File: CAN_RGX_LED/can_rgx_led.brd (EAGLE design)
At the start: 240 x 13 mm, 9 parts

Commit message: board 1_0
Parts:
- added R1: 22M, SparkFun-Resistors:0603
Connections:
- new net N$8: R1.1, U$1.P$2
- net +: now also R1.2; no longer U$1.P$2
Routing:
- added copper zone on layer 1, net N$8
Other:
- board text added: "+"
- board text added: "-"
- board text added: "uORocketry CAN-RGX-24V v1.0"

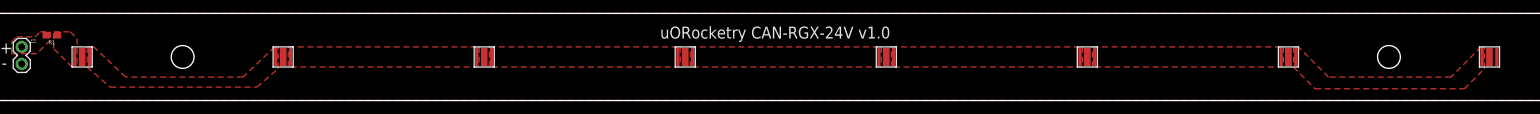
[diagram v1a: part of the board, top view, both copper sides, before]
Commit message: switch LED package
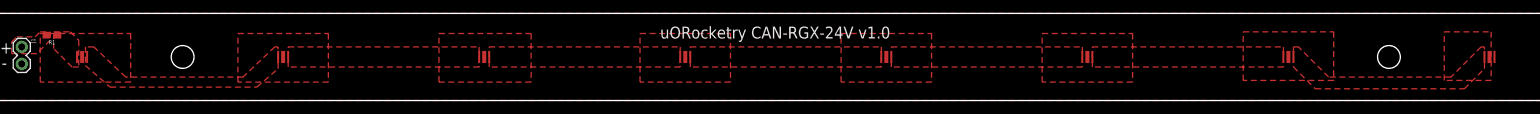
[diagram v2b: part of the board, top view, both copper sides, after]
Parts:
- U$1, U$2, U$3, U$4, U$5, U$6, U$7, U$8: value OSLONSSL150 -> LUXEON-CZ; device uORocketry-parts:OSLONSSL150 -> uORocketry-parts:LUXEON-CZ
- turned U$1 to 0 degrees
- turned U$2 to 0 degrees
- turned U$3 to 0 degrees
- turned U$4 to 0 degrees
- turned U$5 to 0 degrees
- turned U$6 to 0 degrees
- turned U$7 to 0 degrees
- turned U$8 to 0 degrees
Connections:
- new net N$1: U$3.P$1
- new net N$16: U$1.P$1
- new net N$17: U$2.P$1
- new net N$19: U$4.P$1
- new net N$20: U$5.P$1
- new net N$21: U$6.P$1
- new net N$22: U$7.P$1
- new net N$23: U$8.P$1
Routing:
- added copper zone on layer 1, net N$1
- added copper zone on layer 1, net N$16
- added copper zone on layer 1, net N$17
- added copper zone on layer 1, net N$19
- added copper zone on layer 1, net N$20
- added copper zone on layer 1, net N$21
- added copper zone on layer 1, net N$22
- added copper zone on layer 1, net N$23
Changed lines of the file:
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@@
 <?xml version="1.0" encoding="utf-8"?>
 <!DOCTYPE eagle SYSTEM "eagle.dtd">
-<eagle version="9.4.2">
+<eagle version="9.5.2">
 <drawing>
 <settings>
@@
 </autorouter>
 <elements>
-<element name="U$1" library="uORocketry-parts" package="OSLONSSL150" value="OSLONSSL150" x="15" y="6.5" smashed="yes" rot="R90"/>
-<element name="U$2" library="uORocketry-parts" package="OSLONSSL150" value="OSLONSSL150" x="45" y="6.5" smashed="yes" rot="R90"/>
-<element name="U$3" library="uORocketry-parts" package="OSLONSSL150" value="OSLONSSL150" x="75" y="6.5" smashed="yes" rot="R90"/>
-<element name="U$4" library="uORocketry-parts" package="OSLONSSL150" value="OSLONSSL150" x="105" y="6.5" smashed="yes" rot="R90"/>
-<element name="U$5" library="uORocketry-parts" package="OSLONSSL150" value="OSLONSSL150" x="135" y="6.5" smashed="yes" rot="R90"/>
-<element name="U$6" library="uORocketry-parts" package="OSLONSSL150" value="OSLONSSL150" x="165" y="6.5" smashed="yes" rot="R90"/>
-<element name="U$7" library="uORocketry-parts" package="OSLONSSL150" value="OSLONSSL150" x="195" y="6.5" smashed="yes" rot="R90"/>
-<element name="U$8" library="uORocketry-parts" package="OSLONSSL150" value="OSLONSSL150" x="225" y="6.5" smashed="yes" rot="R90"/>
 <element name="J1" library="SparkFun-Connectors" package="1X02" value="" x="6" y="8" smashed="yes" rot="R270">
 <attribute name="NAME" x="7.397" y="9.27" size="0.6096" layer="25" font="vector" ratio="20" rot="R270"/>
@@
 <attribute name="VALUE" x="10.5" y="10.512" size="0.6096" layer="27" font="vector" ratio="20" rot="R180" align="top-center"/>
 </element>
+<element name="U$1" library="uORocketry-parts" package="LUXEON-CZ" value="LUXEON-CZ" x="15" y="6.5" smashed="yes"/>
+<element name="U$2" library="uORocketry-parts" package="LUXEON-CZ" value="LUXEON-CZ" x="45" y="6.5" smashed="yes"/>
+<element name="U$3" library="uORocketry-parts" package="LUXEON-CZ" value="LUXEON-CZ" x="75" y="6.5" smashed="yes"/>
+<element name="U$4" library="uORocketry-parts" package="LUXEON-CZ" value="LUXEON-CZ" x="105" y="6.5" smashed="yes"/>
+<element name="U$5" library="uORocketry-parts" package="LUXEON-CZ" value="LUXEON-CZ" x="135" y="6.5" smashed="yes"/>
+<element name="U$6" library="uORocketry-parts" package="LUXEON-CZ" value="LUXEON-CZ" x="165" y="6.5" smashed="yes"/>
+<element name="U$7" library="uORocketry-parts" package="LUXEON-CZ" value="LUXEON-CZ" x="195" y="6.5" smashed="yes"/>
+<element name="U$8" library="uORocketry-parts" package="LUXEON-CZ" value="LUXEON-CZ" x="225" y="6.5" smashed="yes"/>
 </elements>
 <signals>
-<signal name="N$1">
+<signal name="-">
+<contactref element="J1" pad="2"/>
+<polygon width="0.1524" layer="1" thermals="no" rank="6">
+<vertex x="0" y="13"/>
+<vertex x="0" y="0"/>
+<vertex x="240" y="0"/>
+<vertex x="240" y="13"/>
+</polygon>
+<contactref element="U$8" pad="P$3"/>
+</signal>
+<signal name="N$8">
+<contactref element="R1" pad="1"/>
+<polygon width="0.1524" layer="1" thermals="no">
+<vertex x="10.75" y="10.25"/>
+<vertex x="13.25" y="10.25"/>
+<vertex x="14.5" y="9"/>
+<vertex x="14.5" y="5"/>
+<vertex x="13.5" y="5"/>
+<vertex x="10.75" y="7.75"/>
+</polygon>
+<contactref element="U$1" pad="P$2"/>
+</signal>
+<signal name="+">
+<polygon width="0.1524" layer="1" thermals="no">
+<vertex x="4.5" y="7"/>
+<vertex x="4.5" y="8.75"/>
+<vertex x="5.25" y="9.5"/>
+<vertex x="8" y="9.5"/>
+<vertex x="8.75" y="10.25"/>
+<vertex x="10.25" y="10.25"/>
+<vertex x="10.25" y="9"/>
+<vertex x="8.25" y="7"/>
+</polygon>
+<contactref element="R1" pad="2"/>
+<contactref element="J1" pad="1"/>
+</signal>
+<signal name="N$9">
 <contactref element="U$1" pad="P$3"/>
 <contactref element="U$2" pad="P$2"/>
 <polygon width="0.1524" layer="1" thermals="no">
-<vertex x="15.75" y="5"/>
+<vertex x="15.5" y="5.21875"/>
 <vertex x="19.178571875" y="2"/>
 <vertex x="41.076921875" y="2"/>
@@
 <vertex x="21.5" y="3.5"/>
 <vertex x="16.75" y="8"/>
-<vertex x="15.75" y="8"/>
-</polygon>
-</signal>
-<signal name="N$2">
+<vertex x="15.5" y="8"/>
+</polygon>
+</signal>
+<signal name="N$10">
 <contactref element="U$2" pad="P$3"/>
 <contactref element="U$3" pad="P$2"/>
@@
 </polygon>
 </signal>
-<signal name="N$3">
+<signal name="N$11">
 <contactref element="U$3" pad="P$3"/>
 <contactref element="U$4" pad="P$2"/>
@@
 </polygon>
 </signal>
-<signal name="N$4">
+<signal name="N$12">
 <contactref element="U$4" pad="P$3"/>
 <contactref element="U$5" pad="P$2"/>
@@
 </polygon>
 </signal>
-<signal name="N$5">
+<signal name="N$13">
 <contactref element="U$5" pad="P$3"/>
 <contactref element="U$6" pad="P$2"/>
@@
 </polygon>
 </signal>
-<signal name="N$6">
+<signal name="N$14">
 <contactref element="U$6" pad="P$3"/>
 <contactref element="U$7" pad="P$2"/>
@@
 </polygon>
 </signal>
-<signal name="N$7">
+<signal name="N$15">
 <contactref element="U$7" pad="P$3"/>
 <contactref element="U$8" pad="P$2"/>
@@
 </polygon>
 </signal>
-<signal name="-">
-<contactref element="J1" pad="2"/>
-<contactref element="U$8" pad="P$3"/>
-<polygon width="0.1524" layer="1" thermals="no" rank="6">
-<vertex x="0" y="13"/>
-<vertex x="0" y="0"/>
-<vertex x="240" y="0"/>
-<vertex x="240" y="13"/>
-</polygon>
-</signal>
-<signal name="N$8">
-<contactref element="R1" pad="1"/>
-<contactref element="U$1" pad="P$2"/>
-<polygon width="0.1524" layer="1" thermals="no">
-<vertex x="10.75" y="10.25"/>
-<vertex x="13.25" y="10.25"/>
-<vertex x="14.25" y="9.25"/>
-<vertex x="14.25" y="5"/>
-<vertex x="13.5" y="5"/>
-<vertex x="10.75" y="7.75"/>
-</polygon>
-</signal>
-<signal name="+">
-<polygon width="0.1524" layer="1" thermals="no">
-<vertex x="4.5" y="7"/>
-<vertex x="4.5" y="8.75"/>
-<vertex x="5.25" y="9.5"/>
-<vertex x="8" y="9.5"/>
-<vertex x="8.75" y="10.25"/>
-<vertex x="10.25" y="10.25"/>
-<vertex x="10.25" y="9"/>
-<vertex x="8.25" y="7"/>
-</polygon>
-<contactref element="R1" pad="2"/>
-<contactref element="J1" pad="1"/>
+<signal name="N$16">
+<contactref element="U$1" pad="P$1"/>
+<polygon width="0.1524" layer="1" thermals="no" rank="2">
+<vertex x="8.75" y="10"/>
+<vertex x="22.25" y="10"/>
+<vertex x="22.25" y="2.75"/>
+<vertex x="8.75" y="2.75"/>
+</polygon>
+</signal>
+<signal name="N$17">
+<contactref element="U$2" pad="P$1"/>
+<polygon width="0.1524" layer="1" thermals="no" rank="2">
+<vertex x="38.25" y="10"/>
+<vertex x="51.75" y="10"/>
+<vertex x="51.75" y="2.75"/>
+<vertex x="38.25" y="2.75"/>
+</polygon>
+</signal>
+<signal name="N$1">
+<contactref element="U$3" pad="P$1"/>
+<polygon width="0.1524" layer="1" thermals="no" rank="2">
+<vertex x="68.25" y="10"/>
+<vertex x="82" y="10"/>
+<vertex x="82" y="2.75"/>
+<vertex x="68.25" y="2.75"/>
+</polygon>
+</signal>
+<signal name="N$19">
+<contactref element="U$4" pad="P$1"/>
+<polygon width="0.1524" layer="1" thermals="no" rank="2">
+<vertex x="98.25" y="10"/>
+<vertex x="111.75" y="10"/>
+<vertex x="111.75" y="2.75"/>
+<vertex x="98.25" y="2.75"/>
+</polygon>
+</signal>
+<signal name="N$20">
+<contactref element="U$5" pad="P$1"/>
+<polygon width="0.1524" layer="1" thermals="no" rank="2">
+<vertex x="128.25" y="10"/>
+<vertex x="141.75" y="10"/>
+<vertex x="141.75" y="2.75"/>
+<vertex x="128.25" y="2.75"/>
+</polygon>
+</signal>
+<signal name="N$21">
+<contactref element="U$6" pad="P$1"/>
+<polygon width="0.1524" layer="1" thermals="no" rank="2">
+<vertex x="158.25" y="10"/>
+<vertex x="171.75" y="10"/>
+<vertex x="171.75" y="2.75"/>
+<vertex x="158.25" y="2.75"/>
+</polygon>
+</signal>
+<signal name="N$22">
+<contactref element="U$7" pad="P$1"/>
+<polygon width="0.1524" layer="1" thermals="no" rank="2">
+<vertex x="188.25" y="10.25"/>
+<vertex x="201.75" y="10.25"/>
+<vertex x="201.75" y="3"/>
+<vertex x="188.25" y="3"/>
+</polygon>
+</signal>
+<signal name="N$23">
+<contactref element="U$8" pad="P$1"/>
+<polygon width="0.1524" layer="1" thermals="no" rank="2">
+<vertex x="218.25" y="10.25"/>
+<vertex x="225.25" y="10.25"/>
+<vertex x="225.25" y="3"/>
+<vertex x="218.25" y="3"/>
+</polygon>
 </signal>
 </signals>

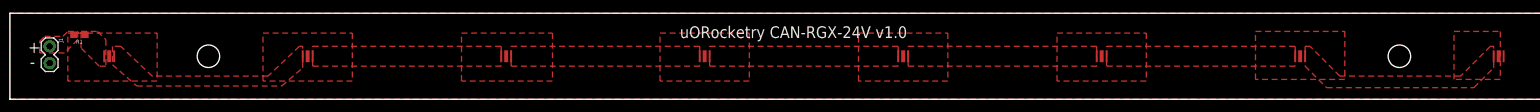
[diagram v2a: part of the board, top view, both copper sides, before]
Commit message: connect middle to anodes as suggested by ayman
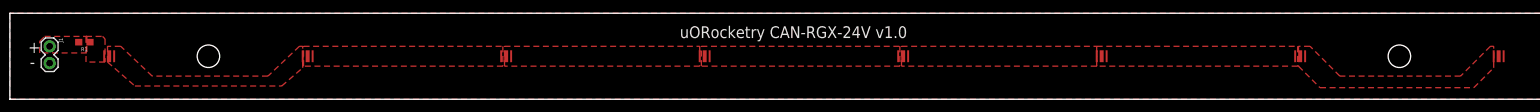
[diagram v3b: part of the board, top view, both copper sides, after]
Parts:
- moved R1 1.35 mm to (11.2, 8.62)
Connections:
- removed net N$10: U$2.P$3, U$3.P$2
- removed net N$11: U$3.P$3, U$4.P$2
- removed net N$12: U$4.P$3, U$5.P$2
- removed net N$13: U$5.P$3, U$6.P$2
- removed net N$14: U$6.P$3, U$7.P$2
- removed net N$15: U$7.P$3, U$8.P$2
- removed net N$23: U$8.P$1
- removed net N$9: U$1.P$3, U$2.P$2
- net -: now also U$8.P$1
- net N$1: now also U$3.P$3, U$4.P$2
- net N$16: now also U$1.P$3, U$2.P$2
- net N$17: now also U$2.P$3, U$3.P$2
- net N$19: now also U$4.P$3, U$5.P$2
- net N$20: now also U$5.P$3, U$6.P$2
- net N$21: now also U$6.P$3, U$7.P$2
- net N$22: now also U$7.P$3, U$8.P$2
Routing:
- removed copper zone on layer 1, net N$10
- removed copper zone on layer 1, net N$11
- removed copper zone on layer 1, net N$12
- removed copper zone on layer 1, net N$13
- removed copper zone on layer 1, net N$14
- removed copper zone on layer 1, net N$15
- removed copper zone on layer 1, net N$23
- removed copper zone on layer 1, net N$9
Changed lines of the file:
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@@
 <?xml version="1.0" encoding="utf-8"?>
 <!DOCTYPE eagle SYSTEM "eagle.dtd">
-<eagle version="9.5.2">
+<eagle version="9.4.2">
 <drawing>
 <settings>
@@
 <setting verticaltext="up"/>
 </settings>
-<grid distance="0.25" unitdist="mm" unit="mm" style="lines" multiple="1" display="yes" altdistance="5" altunitdist="mil" altunit="mil"/>
+<grid distance="0.125" unitdist="mm" unit="mm" style="lines" multiple="1" display="yes" altdistance="5" altunitdist="mil" altunit="mil"/>
 <layers>
 <layer number="1" name="Top" color="4" fill="1" visible="yes" active="yes"/>
@@
 <attribute name="VALUE" x="3.968" y="9.27" size="0.6096" layer="27" font="vector" ratio="20" rot="R270"/>
 </element>
-<element name="R1" library="SparkFun-Resistors" package="0603" value="22M" x="10.5" y="9.75" smashed="yes" rot="R180">
-<attribute name="NAME" x="10.5" y="8.988" size="0.6096" layer="25" font="vector" ratio="20" rot="R180" align="bottom-center"/>
-<attribute name="PROD_ID" value="RES-11132" x="10.5" y="9.75" size="1.778" layer="27" rot="R180" display="off"/>
-<attribute name="VALUE" x="10.5" y="10.512" size="0.6096" layer="27" font="vector" ratio="20" rot="R180" align="top-center"/>
+<element name="R1" library="SparkFun-Resistors" package="0603" value="22M" x="11.25" y="8.625" smashed="yes" rot="R180">
+<attribute name="NAME" x="11.25" y="7.863" size="0.6096" layer="25" font="vector" ratio="20" rot="R180" align="bottom-center"/>
+<attribute name="PROD_ID" value="RES-11132" x="11.25" y="8.625" size="1.778" layer="27" rot="R180" display="off"/>
+<attribute name="VALUE" x="11.25" y="9.387" size="0.6096" layer="27" font="vector" ratio="20" rot="R180" align="top-center"/>
 </element>
 <element name="U$1" library="uORocketry-parts" package="LUXEON-CZ" value="LUXEON-CZ" x="15" y="6.5" smashed="yes"/>
@@
 </polygon>
 <contactref element="U$8" pad="P$3"/>
+<contactref element="U$8" pad="P$1"/>
 </signal>
 <signal name="N$8">
 <contactref element="R1" pad="1"/>
-<polygon width="0.1524" layer="1" thermals="no">
-<vertex x="10.75" y="10.25"/>
-<vertex x="13.25" y="10.25"/>
-<vertex x="14.5" y="9"/>
-<vertex x="14.5" y="5"/>
-<vertex x="13.5" y="5"/>
-<vertex x="10.75" y="7.75"/>
+<polygon width="0.1524" layer="1" thermals="no" rank="2">
+<vertex x="11.5" y="9.5"/>
+<vertex x="14" y="9.5"/>
+<vertex x="14.375" y="9.125"/>
+<vertex x="14.375" y="5.625"/>
+<vertex x="11.5" y="5.625"/>
 </polygon>
 <contactref element="U$1" pad="P$2"/>
 </signal>
 <signal name="+">
-<polygon width="0.1524" layer="1" thermals="no">
+<polygon width="0.1524" layer="1" thermals="no" rank="3">
 <vertex x="4.5" y="7"/>
 <vertex x="4.5" y="8.75"/>
 <vertex x="5.25" y="9.5"/>
-<vertex x="8" y="9.5"/>
-<vertex x="8.75" y="10.25"/>
-<vertex x="10.25" y="10.25"/>
-<vertex x="10.25" y="9"/>
-<vertex x="8.25" y="7"/>
+<vertex x="11.625" y="9.5"/>
+<vertex x="11.625" y="7"/>
 </polygon>
 <contactref element="R1" pad="2"/>
 <contactref element="J1" pad="1"/>
 </signal>
-<signal name="N$9">
+<signal name="N$16">
+<contactref element="U$1" pad="P$1"/>
 <contactref element="U$1" pad="P$3"/>
 <contactref element="U$2" pad="P$2"/>
 <polygon width="0.1524" layer="1" thermals="no">
-<vertex x="15.5" y="5.21875"/>
-<vertex x="19.178571875" y="2"/>
+<vertex x="14.75" y="5.625"/>
+<vertex x="18.89285625" y="2"/>
 <vertex x="41.076921875" y="2"/>
 <vertex x="44.25" y="4.75"/>
@@
 <vertex x="21.5" y="3.5"/>
 <vertex x="16.75" y="8"/>
-<vertex x="15.5" y="8"/>
-</polygon>
-</signal>
-<signal name="N$10">
+<vertex x="14.75" y="8"/>
+</polygon>
+</signal>
+<signal name="N$17">
+<contactref element="U$2" pad="P$1"/>
 <contactref element="U$2" pad="P$3"/>
 <contactref element="U$3" pad="P$2"/>
-<polygon width="0.1524" layer="1" thermals="no">
-<vertex x="45.75" y="8"/>
-<vertex x="74.25" y="8"/>
-<vertex x="74.25" y="5"/>
-<vertex x="45.75" y="5"/>
-</polygon>
-</signal>
-<signal name="N$11">
+<polygon width="0.1524" layer="1" thermals="no" rank="2">
+<vertex x="44.375" y="8"/>
+<vertex x="74.5" y="8"/>
+<vertex x="74.5" y="5"/>
+<vertex x="44.375" y="5"/>
+</polygon>
+</signal>
+<signal name="N$1">
+<contactref element="U$3" pad="P$1"/>
 <contactref element="U$3" pad="P$3"/>
 <contactref element="U$4" pad="P$2"/>
 <polygon width="0.1524" layer="1" thermals="no">
-<vertex x="75.75" y="8"/>
+<vertex x="74.75" y="8"/>
 <vertex x="104.25" y="8"/>
 <vertex x="104.25" y="5"/>
-<vertex x="75.75" y="5"/>
-</polygon>
-</signal>
-<signal name="N$12">
+<vertex x="74.75" y="5"/>
+</polygon>
+</signal>
+<signal name="N$19">
+<contactref element="U$4" pad="P$1"/>
 <contactref element="U$4" pad="P$3"/>
 <contactref element="U$5" pad="P$2"/>
-<polygon width="0.1524" layer="1" thermals="no">
-<vertex x="105.75" y="8"/>
-<vertex x="134.25" y="8"/>
-<vertex x="134.25" y="5"/>
-<vertex x="105.75" y="5"/>
-</polygon>
-</signal>
-<signal name="N$13">
+<polygon width="0.1524" layer="1" thermals="no" rank="2">
+<vertex x="104.5" y="8"/>
+<vertex x="134.5" y="8"/>
+<vertex x="134.5" y="5"/>
+<vertex x="104.5" y="5"/>
+</polygon>
+</signal>
+<signal name="N$20">
+<contactref element="U$5" pad="P$1"/>
 <contactref element="U$5" pad="P$3"/>
 <contactref element="U$6" pad="P$2"/>
 <polygon width="0.1524" layer="1" thermals="no">
-<vertex x="135.75" y="8"/>
+<vertex x="134.75" y="8"/>
 <vertex x="164.25" y="8"/>
 <vertex x="164.25" y="5"/>
-<vertex x="135.75" y="5"/>
-</polygon>
-</signal>
-<signal name="N$14">
+<vertex x="134.75" y="5"/>
+</polygon>
+</signal>
+<signal name="N$21">
+<contactref element="U$6" pad="P$1"/>
 <contactref element="U$6" pad="P$3"/>
 <contactref element="U$7" pad="P$2"/>
-<polygon width="0.1524" layer="1" thermals="no">
-<vertex x="165.75" y="8"/>
-<vertex x="194.25" y="8"/>
-<vertex x="194.25" y="5"/>
-<vertex x="165.75" y="5"/>
-</polygon>
-</signal>
-<signal name="N$15">
+<polygon width="0.1524" layer="1" thermals="no" rank="2">
+<vertex x="164.25" y="8"/>
+<vertex x="194.625" y="8"/>
+<vertex x="194.625" y="5"/>
+<vertex x="164.25" y="5"/>
+</polygon>
+</signal>
+<signal name="N$22">
+<contactref element="U$7" pad="P$1"/>
 <contactref element="U$7" pad="P$3"/>
 <contactref element="U$8" pad="P$2"/>
 <polygon width="0.1524" layer="1" thermals="no">
-<vertex x="195.75" y="5"/>
-<vertex x="199" y="1.75"/>
+<vertex x="194.75" y="5"/>
+<vertex x="198" y="1.75"/>
 <vertex x="221.25" y="1.75"/>
 <vertex x="224.25" y="4.75"/>
@@
 <vertex x="201" y="3.5"/>
 <vertex x="196.5" y="8"/>
-<vertex x="195.75" y="8"/>
-</polygon>
-</signal>
-<signal name="N$16">
-<contactref element="U$1" pad="P$1"/>
-<polygon width="0.1524" layer="1" thermals="no" rank="2">
-<vertex x="8.75" y="10"/>
-<vertex x="22.25" y="10"/>
-<vertex x="22.25" y="2.75"/>
-<vertex x="8.75" y="2.75"/>
-</polygon>
-</signal>
-<signal name="N$17">
-<contactref element="U$2" pad="P$1"/>
-<polygon width="0.1524" layer="1" thermals="no" rank="2">
-<vertex x="38.25" y="10"/>
-<vertex x="51.75" y="10"/>
-<vertex x="51.75" y="2.75"/>
-<vertex x="38.25" y="2.75"/>
-</polygon>
-</signal>
-<signal name="N$1">
-<contactref element="U$3" pad="P$1"/>
-<polygon width="0.1524" layer="1" thermals="no" rank="2">
-<vertex x="68.25" y="10"/>
-<vertex x="82" y="10"/>
-<vertex x="82" y="2.75"/>
-<vertex x="68.25" y="2.75"/>
-</polygon>
-</signal>
-<signal name="N$19">
-<contactref element="U$4" pad="P$1"/>
-<polygon width="0.1524" layer="1" thermals="no" rank="2">
-<vertex x="98.25" y="10"/>
-<vertex x="111.75" y="10"/>
-<vertex x="111.75" y="2.75"/>
-<vertex x="98.25" y="2.75"/>
-</polygon>
-</signal>
-<signal name="N$20">
-<contactref element="U$5" pad="P$1"/>
-<polygon width="0.1524" layer="1" thermals="no" rank="2">
-<vertex x="128.25" y="10"/>
-<vertex x="141.75" y="10"/>
-<vertex x="141.75" y="2.75"/>
-<vertex x="128.25" y="2.75"/>
-</polygon>
-</signal>
-<signal name="N$21">
-<contactref element="U$6" pad="P$1"/>
-<polygon width="0.1524" layer="1" thermals="no" rank="2">
-<vertex x="158.25" y="10"/>
-<vertex x="171.75" y="10"/>
-<vertex x="171.75" y="2.75"/>
-<vertex x="158.25" y="2.75"/>
-</polygon>
-</signal>
-<signal name="N$22">
-<contactref element="U$7" pad="P$1"/>
-<polygon width="0.1524" layer="1" thermals="no" rank="2">
-<vertex x="188.25" y="10.25"/>
-<vertex x="201.75" y="10.25"/>
-<vertex x="201.75" y="3"/>
-<vertex x="188.25" y="3"/>
-</polygon>
-</signal>
-<signal name="N$23">
-<contactref element="U$8" pad="P$1"/>
-<polygon width="0.1524" layer="1" thermals="no" rank="2">
-<vertex x="218.25" y="10.25"/>
-<vertex x="225.25" y="10.25"/>
-<vertex x="225.25" y="3"/>
-<vertex x="218.25" y="3"/>
-</polygon>
-</signal>
+<vertex x="194.75" y="8"/>
+</polygon>
+</signal>
